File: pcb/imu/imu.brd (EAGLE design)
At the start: 14 x 20 mm, 19 parts, among them U2 V_REG_LDOSMD2

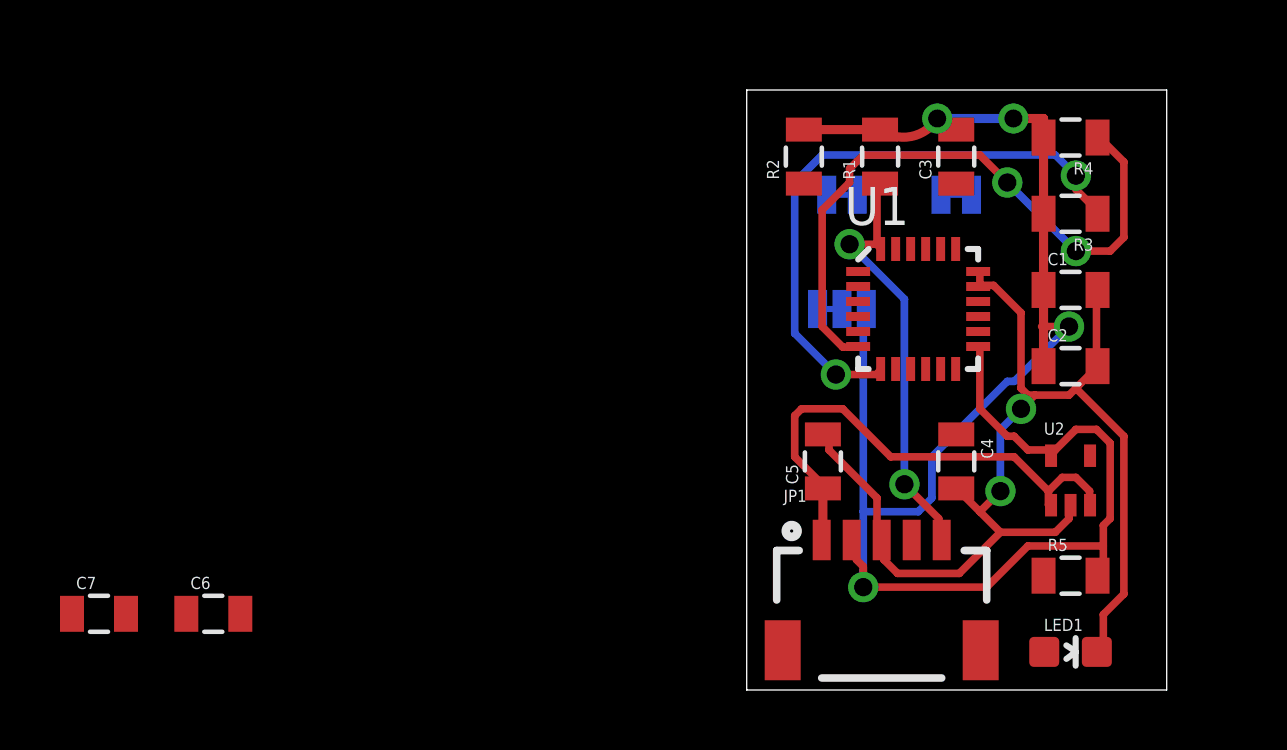
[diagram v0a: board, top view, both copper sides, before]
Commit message: Change LED to 0805 package
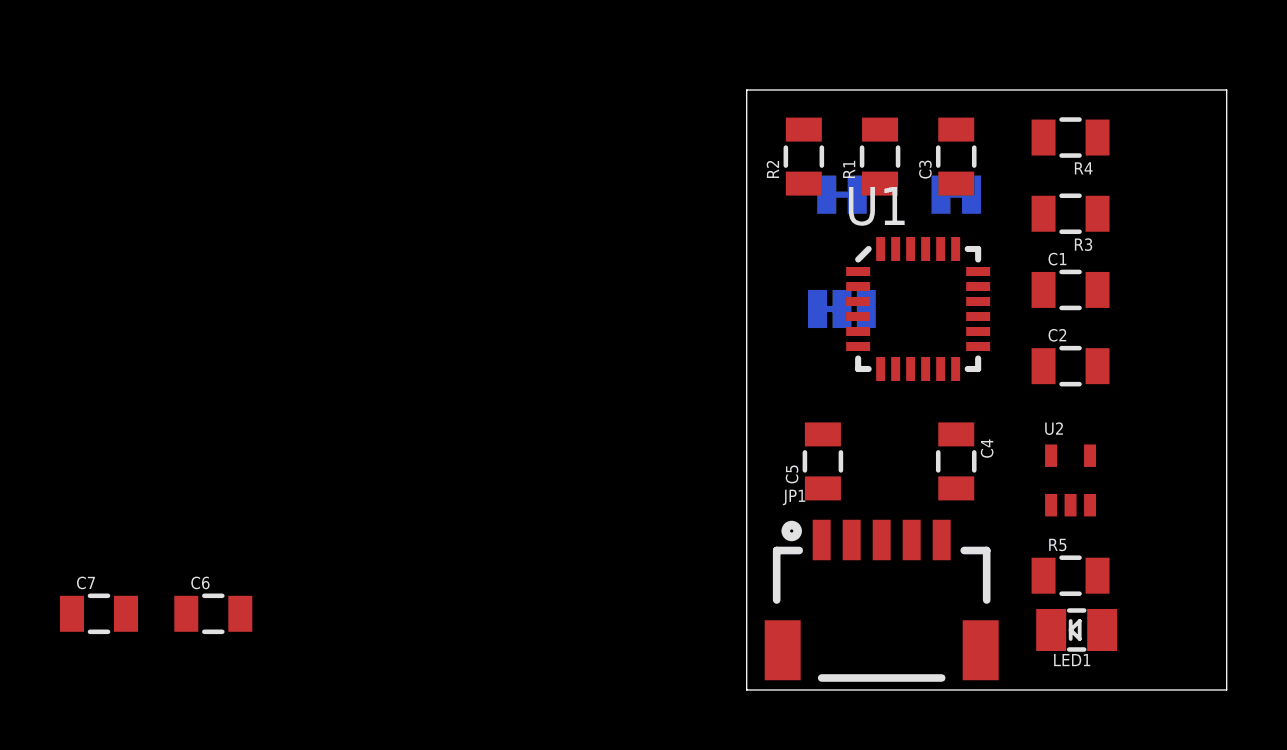
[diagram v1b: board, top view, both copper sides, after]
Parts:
- LED1: device SparkFun-LED:LED-0603 -> SparkFun-LED:LED-0805
- moved LED1 0.76 mm to (11.0, 2.00), turned to 180 degrees
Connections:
- net GND: now also LED1.CATHODE; no longer LED1.C
- net N$1: now also LED1.ANODE; no longer LED1.A
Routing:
- net VCC: track 59.2 -> 0.00 mm, vias 4 -> 0
- net GND: track 39.5 -> 0.00 mm, vias 2 -> 0
- net ESDA: track 21.7 -> 0.00 mm, vias 2 -> 0
- net ESCL: track 20.2 -> 0.00 mm, vias 2 -> 0
- net VIN: track 17.0 -> 0.00 mm
- net SDA: track 14.3 -> 0.00 mm, vias 2 -> 0
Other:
- board size 14 x 20 mm -> 16 x 20 mm

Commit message: Finish MPU board layout revision 1
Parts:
- removed C5: 4.7u, SparkFun-Passives:0805
- removed C6: 10n, SparkFun-Passives:0805
- removed LED1: (no value), SparkFun-LED:LED-0805
- removed R3, R4: 10k, SparkFun-Passives:0805
- removed SJ1, SJ2: JUMPER-PAD-2-NC_BY_TRACE, SparkFun-Passives:PAD-JUMPER-2-NC_BY_TRACE_YES_SILK
- removed SJ3: JUMPER-PAD-3-2OF3_NC_BY_TRACE_SMALL, SparkFun-Passives:PAD-JUMPER-3-2OF3_NC_BY_TRACE_YES_SILK_FULL_BOX
- removed U1: (no value), SparkFun-Sensors:QFN-24-NP
- removed U2: V_REG_LDOSMD2, SparkFun-PowerIC:SC70
- added 3V3_REG: V_REG_LDOSMD, SparkFun-PowerIC:SOT23-5
- added ADDRESS: JUMPER-PAD-3-2OF3_NC_BY_TRACE_SMALL, SparkFun-Passives:PAD-JUMPER-3-2OF3_NC_BY_TRACE_YES_SILK_FULL_BOX
- added C5*: 4.7u, SparkFun-Passives:0805
- added C6*: 470p, SparkFun-Passives:0805
- added CLKIN, FSYNC: JUMPER-PAD-2-NC_BY_TRACE, SparkFun-Passives:PAD-JUMPER-2-NC_BY_TRACE_YES_SILK
- added MPU9150: (no value), SparkFun-Sensors:QFN-24-NP
- added PWR: (no value), SparkFun-LED:LED-0805
- moved C7 26.7 mm to (4.50, 8.00), turned to 90 degrees
- moved R2 6.31 mm to (2.50, 11.5), turned to 180 degrees
- moved R1 4.25 mm to (2.50, 14.0), turned to 180 degrees
- moved C1 2.33 mm to (12.5, 11.8)
- moved C3 2.16 mm to (9.00, 17.0)
- moved C2 2.14 mm to (12.5, 9.50)
- moved R5 1.34 mm to (10.5, 2.50), turned to 90 degrees
- moved C4 0.42 mm to (6.80, 8.00)
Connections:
- net AD0: now also ADDRESS.2, MPU9150.9; no longer SJ3.2, U1.9
- net CLKOUT: now also MPU9150.22; no longer U1.22
- net ESCL: now also MPU9150.7; no longer R3.1, U1.7
- net ESDA: now also MPU9150.6; no longer R4.1, U1.6
- net GND: now also 3V3_REG.2, ADDRESS.3, C5*.2, C6*.2, CLKIN.1, FSYNC.1, MPU9150.15, MPU9150.17, MPU9150.18, PWR.CATHODE; no longer C5.2, C6.2, LED1.CATHODE, SJ1.1, SJ2.1, SJ3.3, U1.15, U1.17, U1.18, U2.2
- net INT: now also MPU9150.12; no longer U1.12
- net N$1: now also PWR.ANODE; no longer LED1.ANODE
- net N$3: now also FSYNC.2, MPU9150.11; no longer SJ1.2, U1.11
- net N$4: now also MPU9150.20; no longer U1.20
- net N$5: now also MPU9150.10; no longer U1.10
- net N$6: now also CLKIN.2, MPU9150.1; no longer SJ2.2, U1.1
- net N$7: now also 3V3_REG.4, C6*.1; no longer C6.1, U2.4
- net SCL: now also MPU9150.23; no longer U1.23
- net SDA: now also MPU9150.24; no longer U1.24
- net VCC: now also 3V3_REG.5, ADDRESS.1, MPU9150.13, MPU9150.3, MPU9150.8; no longer R3.2, R4.2, SJ3.1, U1.13, U1.3, U1.8, U2.5
- net VIN: now also 3V3_REG.1, 3V3_REG.3, C5*.1; no longer C5.1, U2.1, U2.3
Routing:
- net VCC: track 0.00 -> 49.4 mm, vias 0 -> 4
- net SCL: track 0.00 -> 24.4 mm, vias 0 -> 4
- net SDA: track 0.00 -> 22.5 mm, vias 0 -> 2
- net VIN: track 0.00 -> 17.2 mm
- net ESDA: track 0.00 -> 10.1 mm, vias 0 -> 3
- net ESCL: track 0.00 -> 9.35 mm, vias 0 -> 3
- net INT: track 0.00 -> 7.45 mm, vias 0 -> 2
- net N$6: track 0.00 -> 6.95 mm, vias 0 -> 1
- net N$3: track 0.00 -> 5.11 mm, vias 0 -> 1
- net AD0: track 0.00 -> 4.66 mm, vias 0 -> 1
- net N$1: track 0.00 -> 2.52 mm
- net N$5: track 0.00 -> 1.99 mm
- net N$7: track 0.00 -> 1.97 mm
- net N$4: track 0.00 -> 1.91 mm
- added copper zone on layer 1, net GND
- added copper zone on layer 16, net GND
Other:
- board size 16 x 20 mm -> 15 x 20 mm
- board text added: "ESCL"
- board text added: "ESDA"
- board text added: "GND"
- board text added: "INT"
- board text added: "SCL"
- board text added: "SDA"
- board text added: "SELECT"
- board text added: "VCC"
- board text added: "VIN"

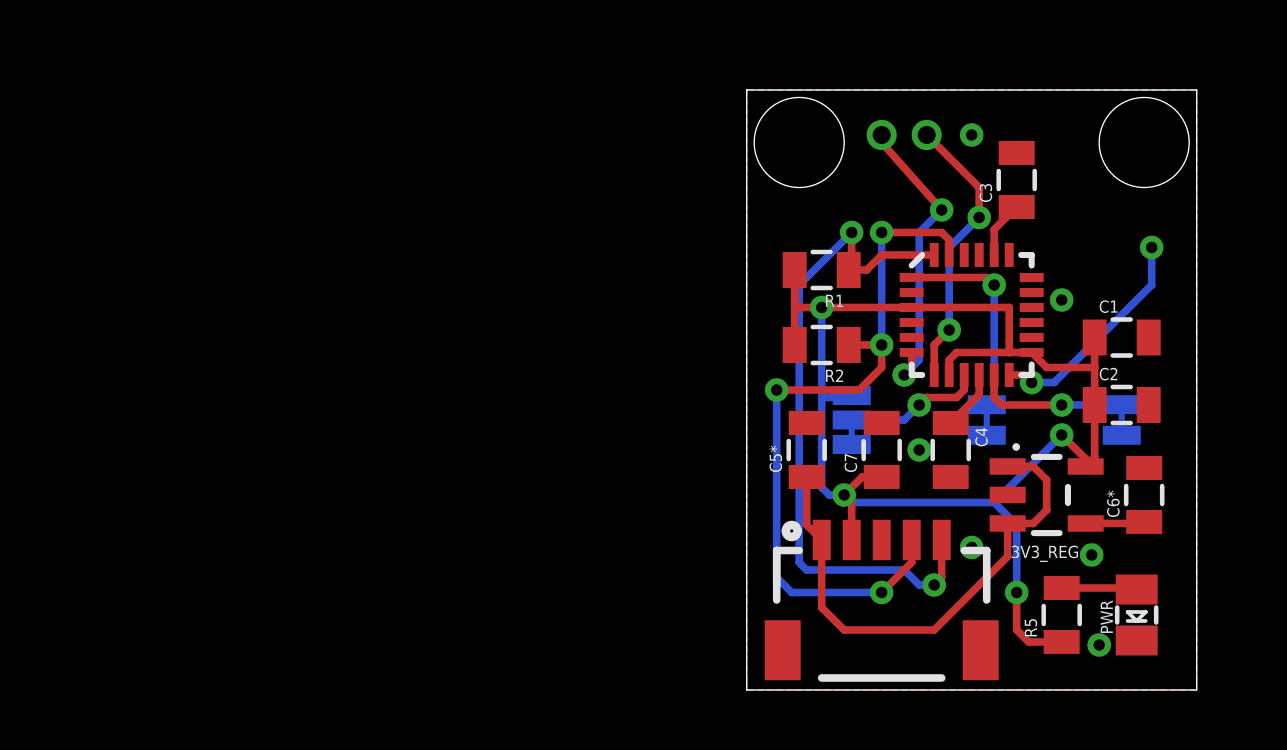
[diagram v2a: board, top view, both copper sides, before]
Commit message: MPU revision 2 with 3mm holes
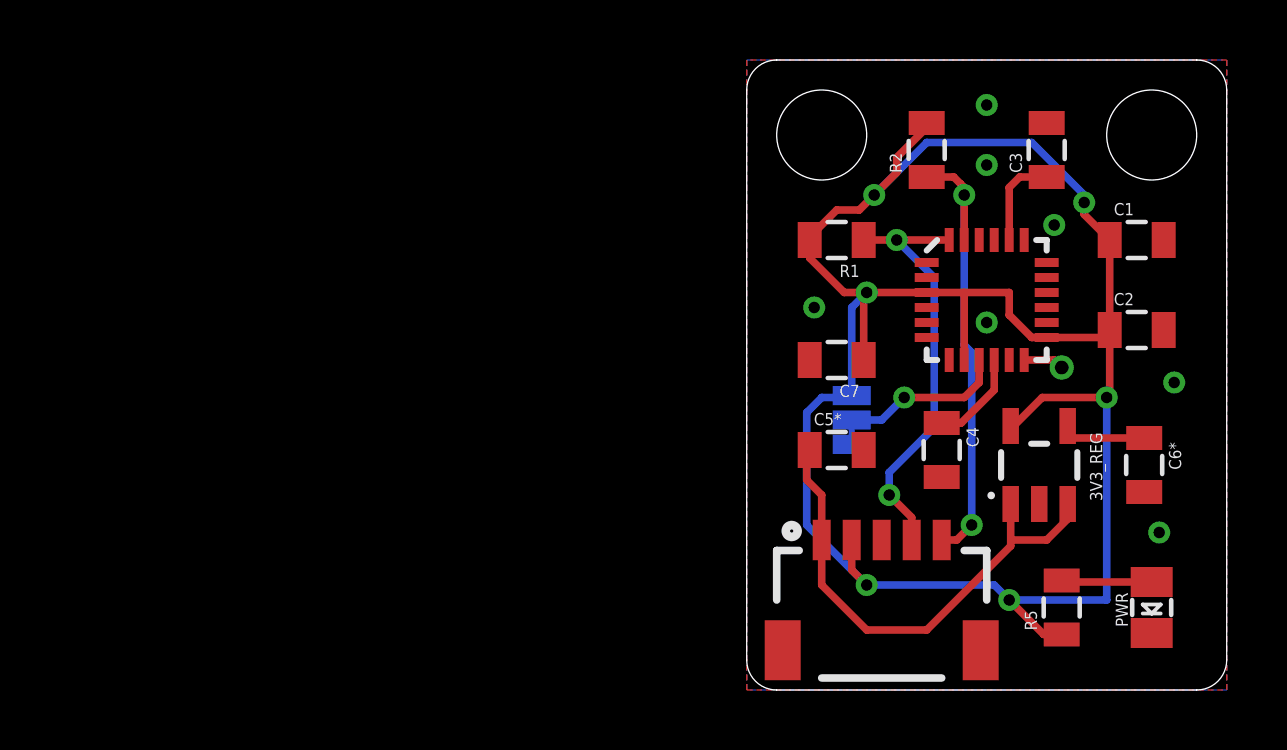
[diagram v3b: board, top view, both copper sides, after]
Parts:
- removed CLKIN, FSYNC: JUMPER-PAD-2-NC_BY_TRACE, SparkFun-Passives:PAD-JUMPER-2-NC_BY_TRACE_YES_SILK
- moved R2 7.38 mm to (6.00, 18.0), turned to 90 degrees
- moved C7 3.35 mm to (3.00, 11.0), turned to 180 degrees
- moved C1 3.29 mm to (13.0, 15.0)
- moved C2 2.55 mm to (13.0, 12.0)
- moved C3 1.41 mm to (10.0, 18.0)
- moved R1 1.12 mm to (3.00, 15.0)
- moved 3V3_REG 1.03 mm to (9.75, 7.50), turned to 0 degrees
- moved C5* 1.00 mm to (3.00, 8.00), turned to 0 degrees
- moved C6* 1.00 mm to (13.2, 7.50), turned to 270 degrees
- moved MPU9150 0.71 mm to (8.00, 13.0)
- moved PWR 0.56 mm to (13.5, 2.75)
- moved C4 0.30 mm to (6.50, 8.00)
- moved R5 0.25 mm to (10.5, 2.75)
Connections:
- removed net N$3: FSYNC.2, MPU9150.11
- removed net N$6: CLKIN.2, MPU9150.1
- net GND: now also MPU9150.1, MPU9150.11; no longer CLKIN.1, FSYNC.1
- net SCL: now also JP1.5; no longer JP1.4
- net SDA: now also JP1.4; no longer JP1.5
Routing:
- net VCC: track 49.4 -> 73.0 mm, vias 4 -> 6
- net ESDA: track 10.1 -> 0.00 mm, vias 3 -> 0
- net ESCL: track 9.35 -> 0.00 mm, vias 3 -> 0
- net SCL: track 24.4 -> 15.5 mm, vias 4 -> 2
- net SDA: track 22.5 -> 14.3 mm
- net N$6: track 6.95 -> 0.00 mm, vias 1 -> 0
- net INT: track 7.45 -> 1.35 mm, vias 2 -> 1
- net N$3: track 5.11 -> 0.00 mm, vias 1 -> 0
- net N$4: track 1.91 -> 3.14 mm
- net N$5: track 1.99 -> 3.21 mm
- net N$7: track 1.97 -> 2.95 mm
- net AD0: track 4.66 -> 5.52 mm
- net N$1: track 2.52 -> 3.05 mm
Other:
- board size 15 x 20 mm -> 16 x 21 mm
- board text removed: "ESCL"
- board text removed: "ESDA"
